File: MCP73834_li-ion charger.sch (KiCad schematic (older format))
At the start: 17 parts, among them CON101 USB-MICRO-B, P102 CONN_01X06, P103 CONN_01X02, P104 CONN_01X02, U101 MCP73834-FCI/UN

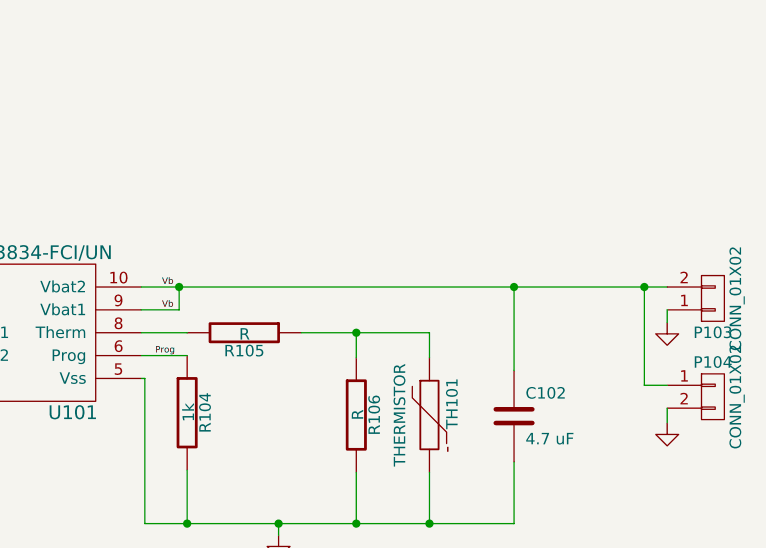
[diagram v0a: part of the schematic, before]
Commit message: changed layout
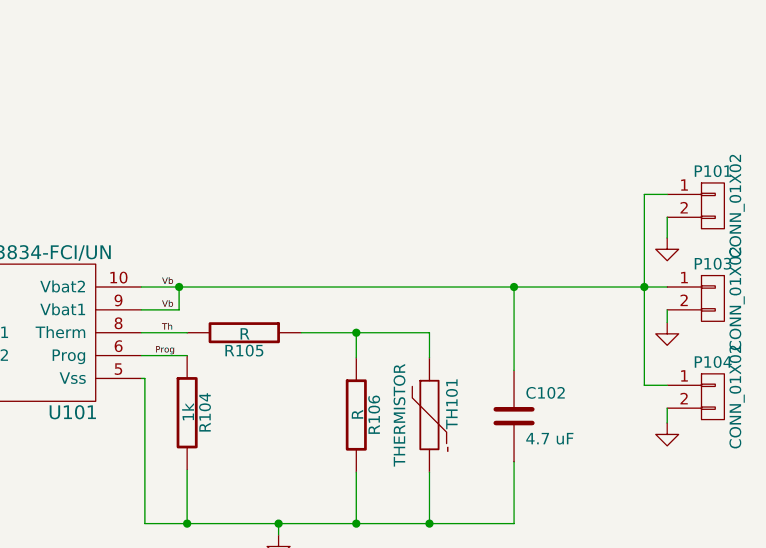
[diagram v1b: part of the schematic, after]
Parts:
- added P101: CONN_01X02, Pin_Headers:Pin_Header_Straight_1x02, symbol CONN_01X02
- U101: footprint Housings_SSOP:MSOP-10_3x3mm_Pitch0.5mm -> (none)
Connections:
- net labels added: Th
- wire segments 56 -> 58
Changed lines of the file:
@@
 F 3 "" H 8750 2955 60  0000 C CNN
 	1    8750 2955
-	1    0    0    1
+	1    0    0    -1
 $EndComp
 $Comp
@@
 	1    0    0    -1
 $EndComp
-Wire Wire Line
-	4820 3105 4820 3055
-Wire Wire Line
-	4820 3105 5250 3105
-Wire Wire Line
-	4570 3205 5250 3205
-Wire Wire Line
-	4570 3055 4570 3205
-Wire Wire Line
-	4320 3055 4320 3305
-Wire Wire Line
-	4320 3305 5250 3305
-Wire Wire Line
-	4570 2435 4570 2555
-Wire Wire Line
-	4820 2435 4820 2555
-Wire Wire Line
-	4820 1930 4820 2035
-Wire Wire Line
-	4570 2035 4570 1930
-Connection ~ 4570 1930
-Wire Wire Line
-	4320 2035 4320 1930
-Connection ~ 4320 1930
-Wire Wire Line
-	3850 2100 3850 1930
-Connection ~ 3850 1930
-Connection ~ 4820 1930
-Wire Wire Line
-	6250 3205 6450 3205
-Wire Wire Line
-	6450 3940 6450 3705
-Wire Wire Line
-	7880 2905 7880 3270
-Connection ~ 7880 2905
-Wire Wire Line
-	7880 3940 7880 3670
-Wire Wire Line
-	6450 3105 6250 3105
-Wire Wire Line
-	6950 3105 7510 3105
-Wire Wire Line
-	7510 3105 7510 3215
-Wire Wire Line
-	7190 3215 7190 3105
-Connection ~ 7190 3105
-Wire Wire Line
-	7190 3940 7190 3715
-Wire Wire Line
-	7510 3940 7510 3715
-Connection ~ 7510 3940
-Connection ~ 7190 3940
-Connection ~ 6450 3940
-Connection ~ 6850 3940
-Wire Wire Line
-	2875 3755 2705 3755
-Wire Wire Line
-	2875 3855 2705 3855
-Wire Wire Line
-	2875 3955 2705 3955
-Wire Wire Line
-	2875 4155 2705 4155
-Wire Wire Line
-	2705 4155 2705 4210
-Wire Wire Line
-	3850 2500 3850 2590
-Wire Wire Line
-	3070 2330 3165 2330
-Wire Wire Line
-	2070 1930 2010 1930
-Wire Wire Line
-	2010 1930 2010 2540
-Wire Wire Line
-	2070 2030 2010 2030
-Wire Wire Line
-	2010 2030 2010 2025
-Connection ~ 2010 2025
-Wire Wire Line
-	2070 2230 2010 2230
-Wire Wire Line
-	2010 2230 2010 2225
-Connection ~ 2010 2225
-Wire Wire Line
-	2070 2330 2010 2330
-Connection ~ 2010 2330
-Wire Wire Line
-	2010 2540 3165 2540
-Connection ~ 3165 2540
-Wire Wire Line
-	8450 3335 8550 3335
-Wire Wire Line
-	8450 2905 8450 3335
-Connection ~ 8450 2905
-Wire Wire Line
-	2875 3655 2705 3655
-Wire Wire Line
-	2875 4055 2700 4055
-Wire Wire Line
-	6250 2905 8550 2905
-Wire Wire Line
-	6250 3005 6415 3005
-Wire Wire Line
-	6250 3305 6265 3305
-Wire Wire Line
-	6265 3305 6265 3940
-Wire Wire Line
-	6265 3940 7880 3940
-Wire Wire Line
-	4320 2435 4320 2555
-Wire Wire Line
-	5250 2905 5195 2905
 NoConn ~ 3070 2230
 NoConn ~ 3070 2130
 NoConn ~ 3070 2030
-Wire Wire Line
-	5195 3005 5250 3005
-Wire Wire Line
-	5195 1930 5195 3005
-Connection ~ 5195 2905
-Wire Wire Line
-	3070 1930 5195 1930
-Wire Wire Line
-	6850 3990 6850 3940
-Wire Wire Line
-	3165 2330 3165 2585
-Wire Wire Line
-	8550 3500 8550 3435
-Wire Wire Line
-	8550 3005 8550 3060
-$Comp
-L MCP73834-FCI/UN U101
-U 1 1 5516C62E
-P 5750 3105
-F 0 "U101" H 5950 2755 60  0000 C CNN
-F 1 "MCP73834-FCI/UN" H 5750 3455 60  0000 C CNN
-F 2 "Housings_SSOP:MSOP-10_3x3mm_Pitch0.5mm" H 5750 3505 60  0001 C CNN
-F 3 "" H 5750 3505 60  0000 C CNN
-	1    5750 3105
-	1    0    0    -1
-$EndComp
 $Comp
 L USB-MICRO-B CON101
@@
 	-1   0    0    -1
 $EndComp
-Wire Wire Line
-	6415 3005 6415 2905
-Connection ~ 6415 2905
 Text Label 6340 3005 0    28   ~ 0
 Vb
 Text Label 3190 1930 0    28   ~ 0
 Vs
+Text Label 6340 3105 0    28   ~ 0
+Th
+$Comp
+L CONN_01X02 P101
+U 1 1 551DA56F
+P 8750 2550
+F 0 "P101" H 8750 2700 50  0000 C CNN
+F 1 "CONN_01X02" V 8850 2550 50  0000 C CNN
+F 2 "Pin_Headers:Pin_Header_Straight_1x02" H 8750 2550 60  0001 C CNN
+F 3 "" H 8750 2550 60  0000 C CNN
+	1    8750 2550
+	1    0    0    -1
+$EndComp
+$Comp
+L GND #PWR07
+U 1 1 551DA780
+P 8550 2690
+F 0 "#PWR07" H 8550 2440 60  0001 C CNN
+F 1 "GND" H 8550 2540 60  0001 C CNN
+F 2 "" H 8550 2690 60  0000 C CNN
+F 3 "" H 8550 2690 60  0000 C CNN
+F 4 "Value" H 8550 2690 60  0001 C CNN "MPN"
+	1    8550 2690
+	1    0    0    -1
+$EndComp
+Wire Wire Line
+	4820 3105 4820 3055
+Wire Wire Line
+	4820 3105 5250 3105
+Wire Wire Line
+	4570 3205 5250 3205
+Wire Wire Line
+	4570 3055 4570 3205
+Wire Wire Line
+	4320 3055 4320 3305
+Wire Wire Line
+	4320 3305 5250 3305
+Wire Wire Line
+	4570 2435 4570 2555
+Wire Wire Line
+	4820 2435 4820 2555
+Wire Wire Line
+	4820 1930 4820 2035
+Wire Wire Line
+	4570 2035 4570 1930
+Connection ~ 4570 1930
+Wire Wire Line
+	4320 2035 4320 1930
+Connection ~ 4320 1930
+Wire Wire Line
+	3850 2100 3850 1930
+Connection ~ 3850 1930
+Connection ~ 4820 1930
+Wire Wire Line
+	6250 3205 6450 3205
+Wire Wire Line
+	6450 3940 6450 3705
+Wire Wire Line
+	7880 2905 7880 3270
+Connection ~ 7880 2905
+Wire Wire Line
+	7880 3940 7880 3670
+Wire Wire Line
+	6450 3105 6250 3105
+Wire Wire Line
+	6950 3105 7510 3105
+Wire Wire Line
+	7510 3105 7510 3215
+Wire Wire Line
+	7190 3215 7190 3105
+Connection ~ 7190 3105
+Wire Wire Line
+	7190 3940 7190 3715
+Wire Wire Line
+	7510 3940 7510 3715
+Connection ~ 7510 3940
+Connection ~ 7190 3940
+Connection ~ 6450 3940
+Connection ~ 6850 3940
+Wire Wire Line
+	2875 3755 2705 3755
+Wire Wire Line
+	2875 3855 2705 3855
+Wire Wire Line
+	2875 3955 2705 3955
+Wire Wire Line
+	2875 4155 2705 4155
+Wire Wire Line
+	2705 4155 2705 4210
+Wire Wire Line
+	3850 2500 3850 2590
+Wire Wire Line
+	3070 2330 3165 2330
+Wire Wire Line
+	2070 1930 2010 1930
+Wire Wire Line
+	2010 1930 2010 2540
+Wire Wire Line
+	2070 2030 2010 2030
+Wire Wire Line
+	2010 2030 2010 2025
+Connection ~ 2010 2025
+Wire Wire Line
+	2070 2230 2010 2230
+Wire Wire Line
+	2010 2230 2010 2225
+Connection ~ 2010 2225
+Wire Wire Line
+	2070 2330 2010 2330
+Connection ~ 2010 2330
+Wire Wire Line
+	2010 2540 3165 2540
+Connection ~ 3165 2540
+Wire Wire Line
+	8450 3335 8550 3335
+Wire Wire Line
+	8450 2500 8450 3335
+Connection ~ 8450 2905
+Wire Wire Line
+	2875 3655 2705 3655
+Wire Wire Line
+	2875 4055 2700 4055
+Wire Wire Line
+	6250 2905 8550 2905
+Wire Wire Line
+	6250 3005 6415 3005
+Wire Wire Line
+	6250 3305 6265 3305
+Wire Wire Line
+	6265 3305 6265 3940
+Wire Wire Line
+	6265 3940 7880 3940
+Wire Wire Line
+	4320 2435 4320 2555
+Wire Wire Line
+	5250 2905 5195 2905
+Wire Wire Line
+	5195 3005 5250 3005
+Wire Wire Line
+	5195 1930 5195 3005
+Connection ~ 5195 2905
+Wire Wire Line
+	3070 1930 5195 1930
+Wire Wire Line
+	6850 3990 6850 3940
+Wire Wire Line
+	3165 2330 3165 2585
+Wire Wire Line
+	8550 3500 8550 3435
+Wire Wire Line
+	8550 3005 8550 3060
+Wire Wire Line
+	6415 3005 6415 2905
+Connection ~ 6415 2905
+Wire Wire Line
+	8550 2500 8450 2500
+Wire Wire Line
+	8550 2600 8550 2690
+$Comp
+L MCP73834-FCI/UN U101
+U 1 1 551DA7A4
+P 5750 3105
+F 0 "U101" H 5950 2755 60  0000 C CNN
+F 1 "MCP73834-FCI/UN" H 5750 3455 60  0000 C CNN
+F 2 "" H 5750 3505 60  0000 C CNN
+F 3 "" H 5750 3505 60  0000 C CNN
+	1    5750 3105
+	1    0    0    -1
+$EndComp
 $EndSCHEMATC
